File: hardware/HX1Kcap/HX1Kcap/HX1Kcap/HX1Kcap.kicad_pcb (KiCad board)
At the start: 2 copper layers, 124.5 x 96.5 mm, 72 parts, among them J1 Conn_02x05_Odd_Even, J2 Conn_01x20_Male, J5 Conn_01x20_Male, J6 Conn_01x03_Male, U1 LTC3406ES5, U2 AT25SF081-SSHD-X, U3 ICE40HX1K-VQ100(VQFP100)

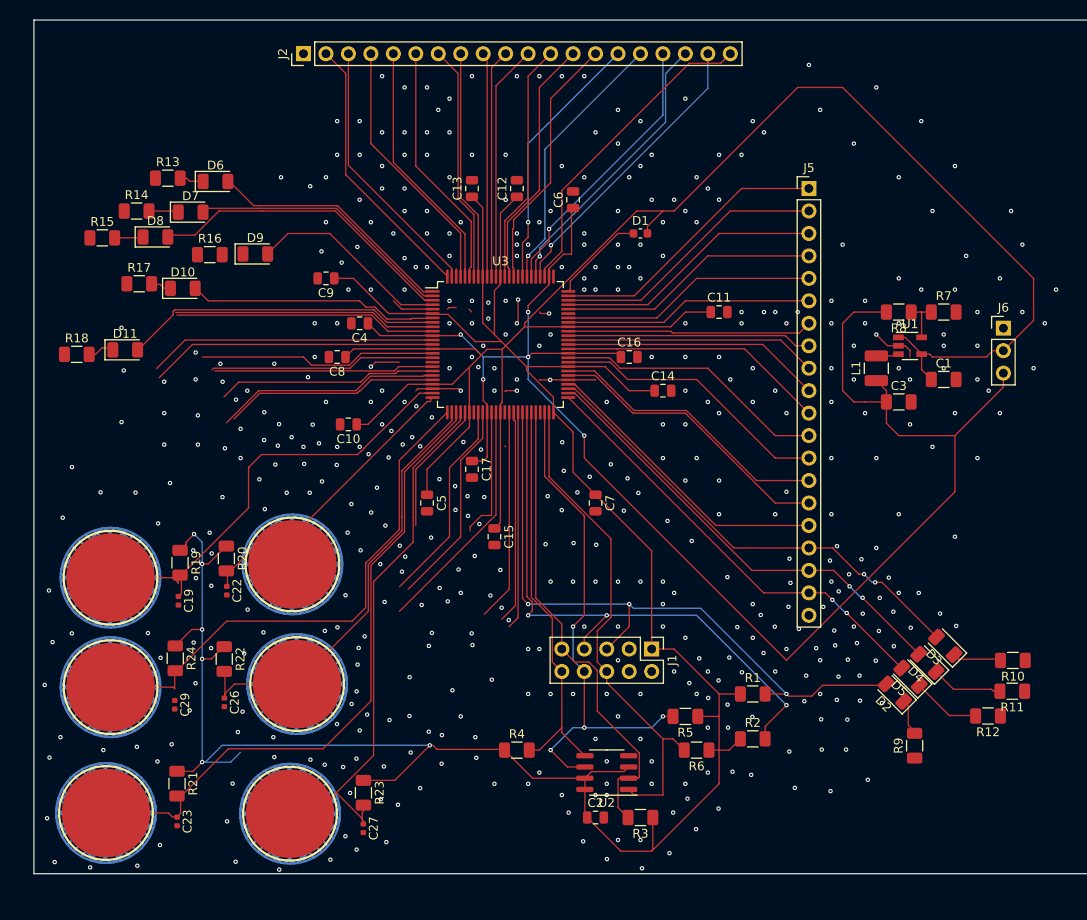
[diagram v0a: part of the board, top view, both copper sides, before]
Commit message: ice40HX1K capSense board fixed errors in the PCB
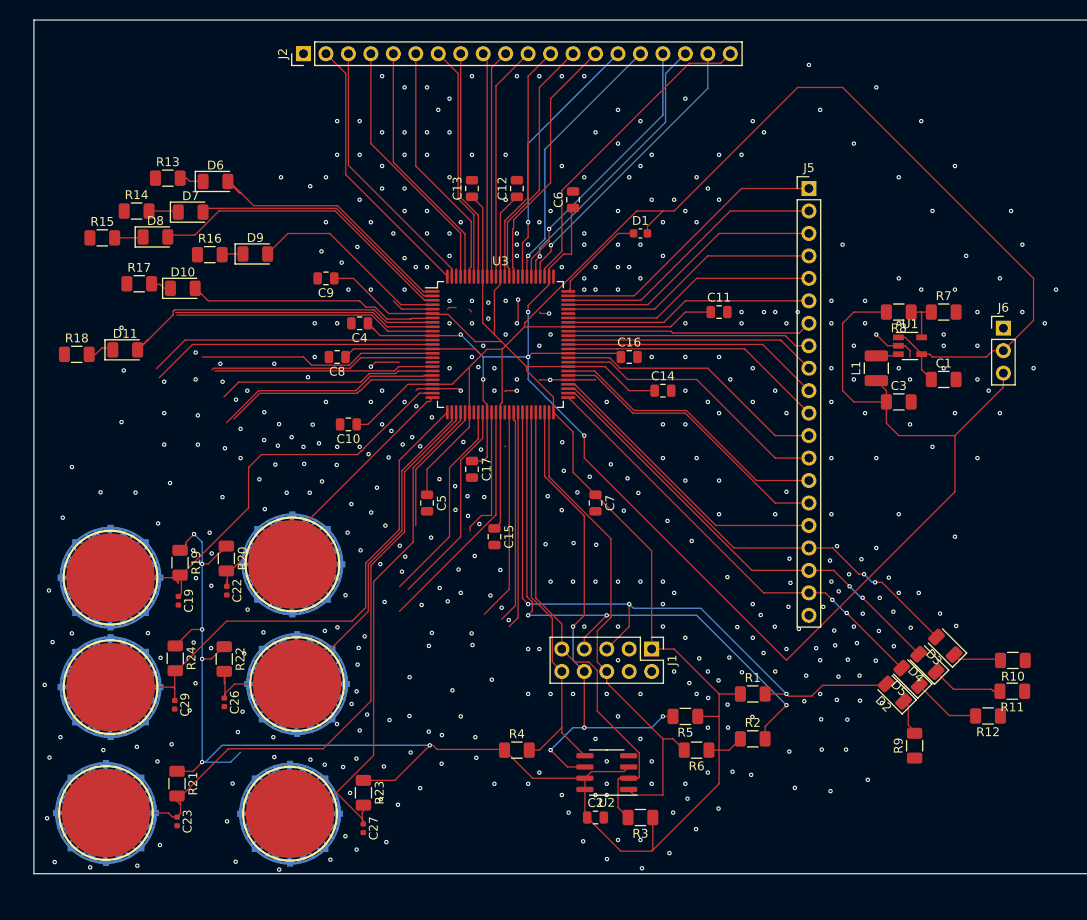
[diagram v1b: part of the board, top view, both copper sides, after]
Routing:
- net IO25: track 32.9 -> 36.6 mm
- net IO1: track 27.7 -> 30.4 mm
- net +3V3: track 482.7 -> 485.2 mm
- net Net-(D9-Pad1): track 0.00 -> 2.37 mm
- net IO26: track 59.7 -> 61.8 mm
- net IO29: track 59.3 -> 61.4 mm
- net IO27: track 49.6 -> 51.6 mm
- net IO8: track 36.0 -> 37.6 mm
- net +1V2: track 185.3 -> 186.6 mm
- net IO28: track 73.3 -> 74.5 mm
- net IO7: track 28.5 -> 29.5 mm
- net IO54: track 33.1 -> 33.8 mm
